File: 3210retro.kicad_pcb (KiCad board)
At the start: 6 copper layers, 44 x 118 mm, 197 parts, among them J1101 MICRO_SD_HINGE, J801 TEST_2P, P101 USB_OTG, P103 LIPO, P104 DC, P106 SPEAKER, P107 HEADPHONE, P108 RUMBLE, P301 SEPS525, P801 JTAG, Q501 MMBF170, Q701 MMBF170, SW701 SW_PUSH, SW702 C, SW703 1, SW704 4ghi, SW705 7pqrs, SW706 -, SW707 2abc, SW708 5jkl, SW709 8tuv, SW710 UP, SW711 3def, SW712 6mno, SW713 9wxyz, SW714 *+, SW715 DOWN, SW716 0space, SW717 #up, U1301 LSM9DS1, U201 MAX1555, U202 TPS62742, U203 TPS61021A, U301 TPS61041DBV, U401 TLV320ADC3101, U402 DRV8601, U403 TLV320DAC3100, U404 MP34DT01TR, U405 MP34DT01TR, U504 A7, U505 SIM_SLOT, U601 ESP-12E, U801 STM32F756VGTx, X101 ANT_GPS, X102 ANT_GSM, Y801 32kHz, Y802 24MHz

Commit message: Current version that was ordered as board version 1
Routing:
- net GNDA: vias 13 -> 14
- net GND: vias 141 -> 139
- net /Audio Amplifier/HPL: vias 3 -> 4
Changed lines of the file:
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@@
   )
   (setup
-    (last_trace_width 0.2)
+    (last_trace_width 0.25)
     (user_trace_width 0.125)
     (user_trace_width 0.2)
@@
     (mod_text_size 1 1)
     (mod_text_width 0.15)
-    (pad_size 1.725 1.725)
-    (pad_drill 0)
+    (pad_size 0.31 0.31)
+    (pad_drill 0.3)
     (pad_to_mask_clearance 0.1)
     (aux_axis_origin 0 0)
@@
     (fp_line (start -1.2 -1.5) (end 1.2 -1.5) (layer B.SilkS) (width 0.15))
     (fp_line (start -1.2 1.5) (end -1.2 -1.5) (layer B.SilkS) (width 0.15))
-    (pad 13 thru_hole circle (at 0 -0.75 270) (size 0.21 0.21) (drill 0.2) (layers *.Cu *.Mask)
+    (pad 13 thru_hole circle (at 0 -0.75 270) (size 0.31 0.31) (drill 0.3) (layers *.Cu *.Mask)
       (net 1 GND))
-    (pad 13 thru_hole circle (at 0 0.75 270) (size 0.21 0.21) (drill 0.2) (layers *.Cu *.Mask)
+    (pad 13 thru_hole circle (at 0 0.75 270) (size 0.31 0.31) (drill 0.3) (layers *.Cu *.Mask)
       (net 1 GND))
-    (pad 13 thru_hole circle (at 0 0 270) (size 0.21 0.21) (drill 0.2) (layers *.Cu *.Mask)
+    (pad 13 thru_hole circle (at 0 0 270) (size 0.31 0.31) (drill 0.3) (layers *.Cu *.Mask)
       (net 1 GND))
     (pad 13 smd roundrect (at 0 0 270) (size 0.9 2) (layers B.Cu B.Paste B.Mask)(roundrect_rratio 0.2)
@@
   (via (at 94.95 158.04) (size 0.5) (drill 0.3) (layers F.Cu B.Cu) (net 1))
   (via (at 89.82 158.49) (size 0.5) (drill 0.3) (layers F.Cu B.Cu) (net 1))
-  (via (at 93.83 156.09) (size 0.5) (drill 0.3) (layers F.Cu B.Cu) (net 1))
+  (via (at 93.83 156.09) (size 0.5) (drill 0.3) (layers F.Cu B.Cu) (net 20))
   (via (at 90.2 153.79) (size 0.5) (drill 0.3) (layers F.Cu B.Cu) (net 1))
-  (via (at 93.65 148.96) (size 0.5) (drill 0.3) (layers F.Cu B.Cu) (net 1))
+  (via (at 93.65 148.96) (size 0.5) (drill 0.3) (layers F.Cu B.Cu) (net 18))
   (via (at 117.84 148.1) (size 0.5) (drill 0.3) (layers F.Cu B.Cu) (net 1))
   (via (at 92.54 143.33) (size 0.5) (drill 0.3) (layers F.Cu B.Cu) (net 1))

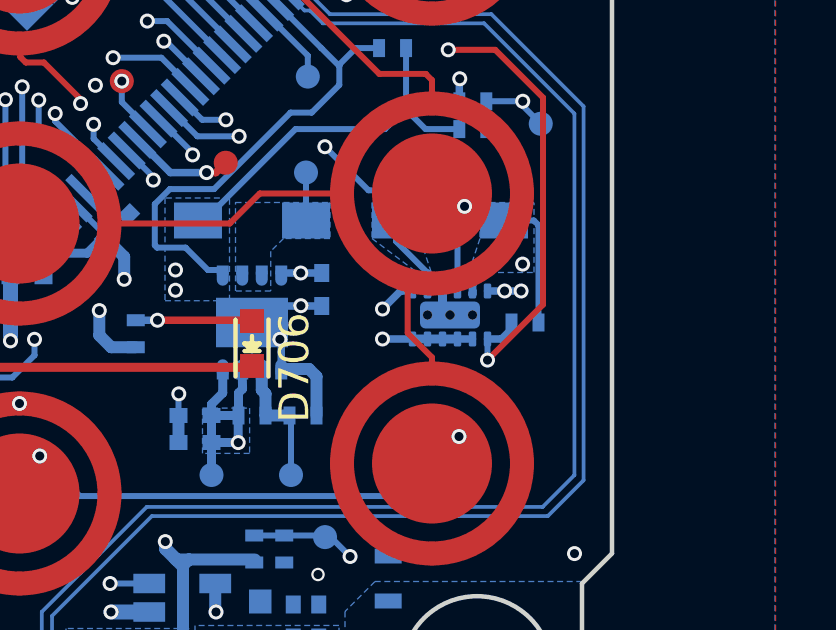
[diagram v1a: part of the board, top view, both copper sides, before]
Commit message: Revert "Current version that was ordered as board version 1"
This reverts commit 2e223613ce4d310fd76aa4487f7c9213e834245a.
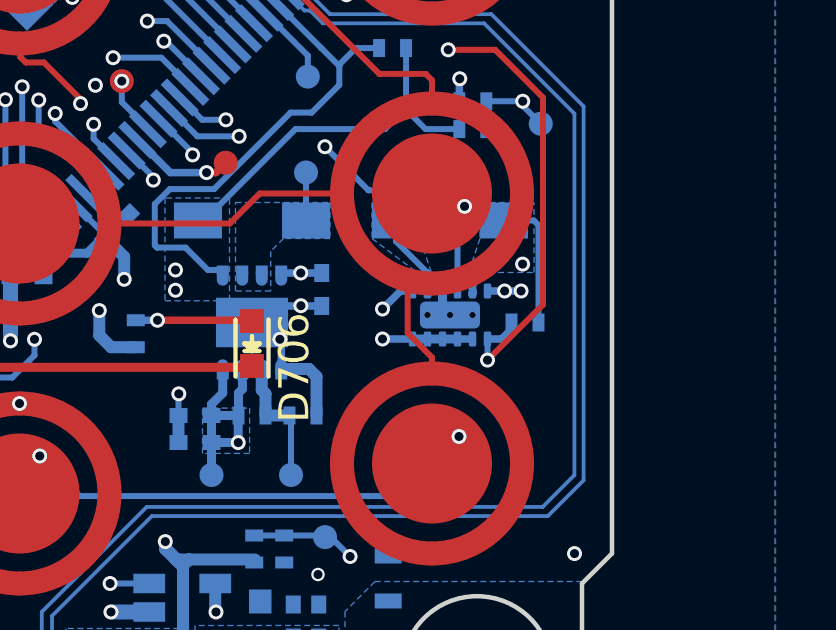
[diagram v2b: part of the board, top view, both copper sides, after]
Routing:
- net GNDA: vias 14 -> 13
- net GND: vias 139 -> 141
- net /Audio Amplifier/HPL: vias 4 -> 3
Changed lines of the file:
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@@
   )
   (setup
-    (last_trace_width 0.25)
+    (last_trace_width 0.2)
     (user_trace_width 0.125)
     (user_trace_width 0.2)
@@
     (mod_text_size 1 1)
     (mod_text_width 0.15)
-    (pad_size 0.31 0.31)
-    (pad_drill 0.3)
+    (pad_size 1.725 1.725)
+    (pad_drill 0)
     (pad_to_mask_clearance 0.1)
     (aux_axis_origin 0 0)
@@
     (fp_line (start -1.2 -1.5) (end 1.2 -1.5) (layer B.SilkS) (width 0.15))
     (fp_line (start -1.2 1.5) (end -1.2 -1.5) (layer B.SilkS) (width 0.15))
-    (pad 13 thru_hole circle (at 0 -0.75 270) (size 0.31 0.31) (drill 0.3) (layers *.Cu *.Mask)
+    (pad 13 thru_hole circle (at 0 -0.75 270) (size 0.21 0.21) (drill 0.2) (layers *.Cu *.Mask)
       (net 1 GND))
-    (pad 13 thru_hole circle (at 0 0.75 270) (size 0.31 0.31) (drill 0.3) (layers *.Cu *.Mask)
+    (pad 13 thru_hole circle (at 0 0.75 270) (size 0.21 0.21) (drill 0.2) (layers *.Cu *.Mask)
       (net 1 GND))
-    (pad 13 thru_hole circle (at 0 0 270) (size 0.31 0.31) (drill 0.3) (layers *.Cu *.Mask)
+    (pad 13 thru_hole circle (at 0 0 270) (size 0.21 0.21) (drill 0.2) (layers *.Cu *.Mask)
       (net 1 GND))
     (pad 13 smd roundrect (at 0 0 270) (size 0.9 2) (layers B.Cu B.Paste B.Mask)(roundrect_rratio 0.2)
@@
   (via (at 94.95 158.04) (size 0.5) (drill 0.3) (layers F.Cu B.Cu) (net 1))
   (via (at 89.82 158.49) (size 0.5) (drill 0.3) (layers F.Cu B.Cu) (net 1))
-  (via (at 93.83 156.09) (size 0.5) (drill 0.3) (layers F.Cu B.Cu) (net 20))
+  (via (at 93.83 156.09) (size 0.5) (drill 0.3) (layers F.Cu B.Cu) (net 1))
   (via (at 90.2 153.79) (size 0.5) (drill 0.3) (layers F.Cu B.Cu) (net 1))
-  (via (at 93.65 148.96) (size 0.5) (drill 0.3) (layers F.Cu B.Cu) (net 18))
+  (via (at 93.65 148.96) (size 0.5) (drill 0.3) (layers F.Cu B.Cu) (net 1))
   (via (at 117.84 148.1) (size 0.5) (drill 0.3) (layers F.Cu B.Cu) (net 1))
   (via (at 92.54 143.33) (size 0.5) (drill 0.3) (layers F.Cu B.Cu) (net 1))

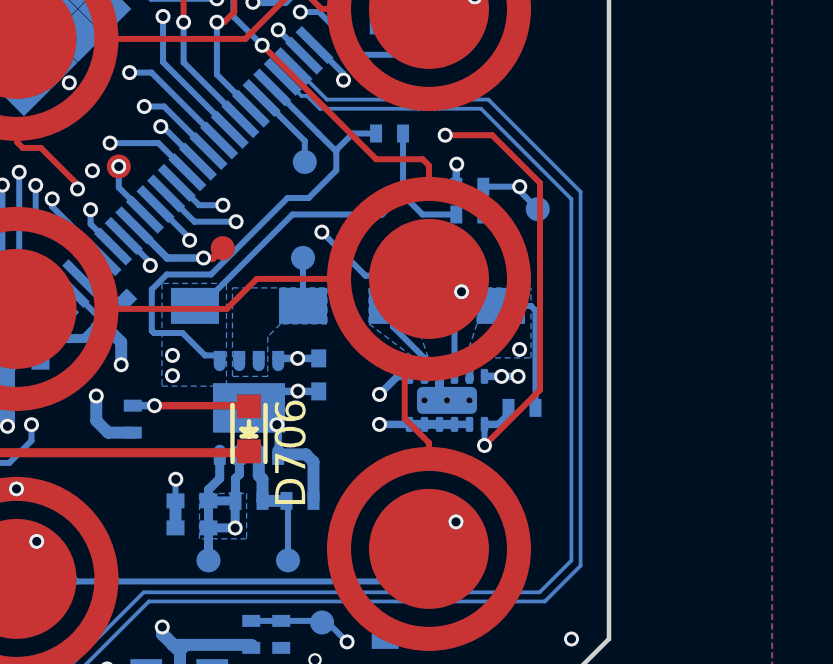
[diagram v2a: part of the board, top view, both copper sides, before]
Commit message: Modified Layout of U202 and added 10uF capacitor to output of U202 3V3 net is set top be 3V
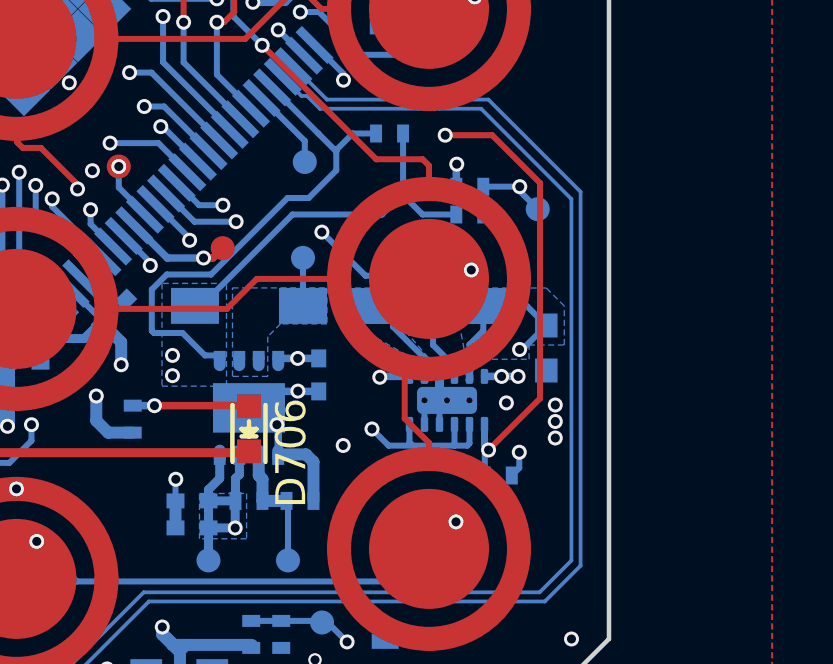
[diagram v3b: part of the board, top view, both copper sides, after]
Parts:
- added C201: 10u, Capacitors_SMD:C_0603, B.Cu at (117.0, 138.4)
- moved R215 2.39 mm to (115.4, 142.7)
- moved L202 0.59 mm to (113.1, 137.0)
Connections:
- U202 pad 10: +BATT_LIPO -> GND
- U202 pad 11: +BATT_LIPO -> GND
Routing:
- net 3V3: track 206.3 -> 210.0 mm, vias 10 -> 11
- net +BATT_LIPO: track 85.9 -> 88.3 mm
- net GND: track 200.0 -> 201.7 mm, vias 141 -> 146
- net /Buttons and LEDs/KEYPAD_COL2: track 66.0 -> 65.1 mm
- net /Power and Battery/3V3_PG: track 34.5 -> 35.2 mm
